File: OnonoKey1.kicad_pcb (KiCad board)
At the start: 2 copper layers, 85 parts, among them SW00 Switch, SW01 Switch, SW02 Switch, SW03 Switch, SW04 Switch, SW05 Switch, SW06 Switch, SW10 Switch, SW11 Switch, SW12 Switch, SW13 Switch, SW14 Switch, SW15 Switch, SW16 Switch, SW20 Switch, SW21 Switch, SW22 Switch, SW23 Switch, SW24 Switch, SW25 Switch, SW26 Switch, SW30 Switch, SW31 Switch, SW32 Switch, SW33 Switch, SW34 Switch, SW35 Switch, SW36 Switch, SW40 Switch, SW41 Switch, SW42 Switch, SW43 Switch, SW44 Switch, SW45 Switch, SW46 Switch, SW50 Switch, SW51 Switch, SW52 Switch, SW53 Switch, SW54 Switch, SW55 Switch, SW56 Switch, U1 RP2040_Zero

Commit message: Changed footprints, rearranged keys on pcb
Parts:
- SW00, SW01, SW02, SW03, SW04, SW05, SW06, SW10, SW11, SW12, SW13, SW14, SW15, SW16, SW20, SW21, SW22, SW23, SW24, SW25, SW26, SW30, SW31, SW32, SW33, SW34, SW35, SW36, SW40, SW41, SW42, SW43, SW44, SW45, SW46, SW50, SW51, SW52, SW53, SW54, SW55, SW56: footprint ScottoKeebs_MX:MX_PCB_1.00u -> Daprice_Keyswitches:Kailh_socket_MX_optional_reversible_1u
- moved SW51 171.1 mm to (60.7, 156.2)
- moved SW41 156.6 mm to (60.7, 137.2)
- moved SW52 154.5 mm to (79.7, 143.2)
- moved SW26 147.3 mm to (155.9, 86.1)
- moved SW31 144.8 mm to (60.7, 118.2)
- moved SW42 144.2 mm to (79.7, 124.2)
- moved SW53 140.7 mm to (98.8, 140.2)
- moved SW32 137.5 mm to (79.7, 105.2)
- moved SW25 136.6 mm to (136.9, 86.1)
- moved SW36 135.2 mm to (155.9, 105.2)
- moved SW43 134.2 mm to (98.8, 121.2)
- moved SW33 132.1 mm to (98.8, 102.2)
- moved SW21 130.7 mm to (60.7, 99.1)
- moved SW22 129.8 mm to (79.7, 86.1)
- moved SW24 129.8 mm to (117.8, 86.1)
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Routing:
- net /COL0: track 177.2 -> 0.00 mm
- net /COL1: track 158.9 -> 0.00 mm
- net /ROW1: track 114.3 -> 0.00 mm
- net /ROW0: track 114.3 -> 0.00 mm
- net /COL6: track 19.1 -> 0.00 mm
- net /COL5: track 19.1 -> 0.00 mm
- net /COL4: track 19.1 -> 0.00 mm
- net /COL3: track 19.1 -> 0.00 mm
- net /COL2: track 19.1 -> 0.00 mm
- net Net-(D6-A): track 8.43 -> 0.00 mm
- net Net-(D4-A): track 8.43 -> 0.00 mm
- net Net-(D2-A): track 8.43 -> 0.00 mm
- net Net-(D13-A): track 8.43 -> 0.00 mm
- net Net-(D1-A): track 8.43 -> 0.00 mm
- net Net-(D8-A): track 8.43 -> 0.00 mm
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
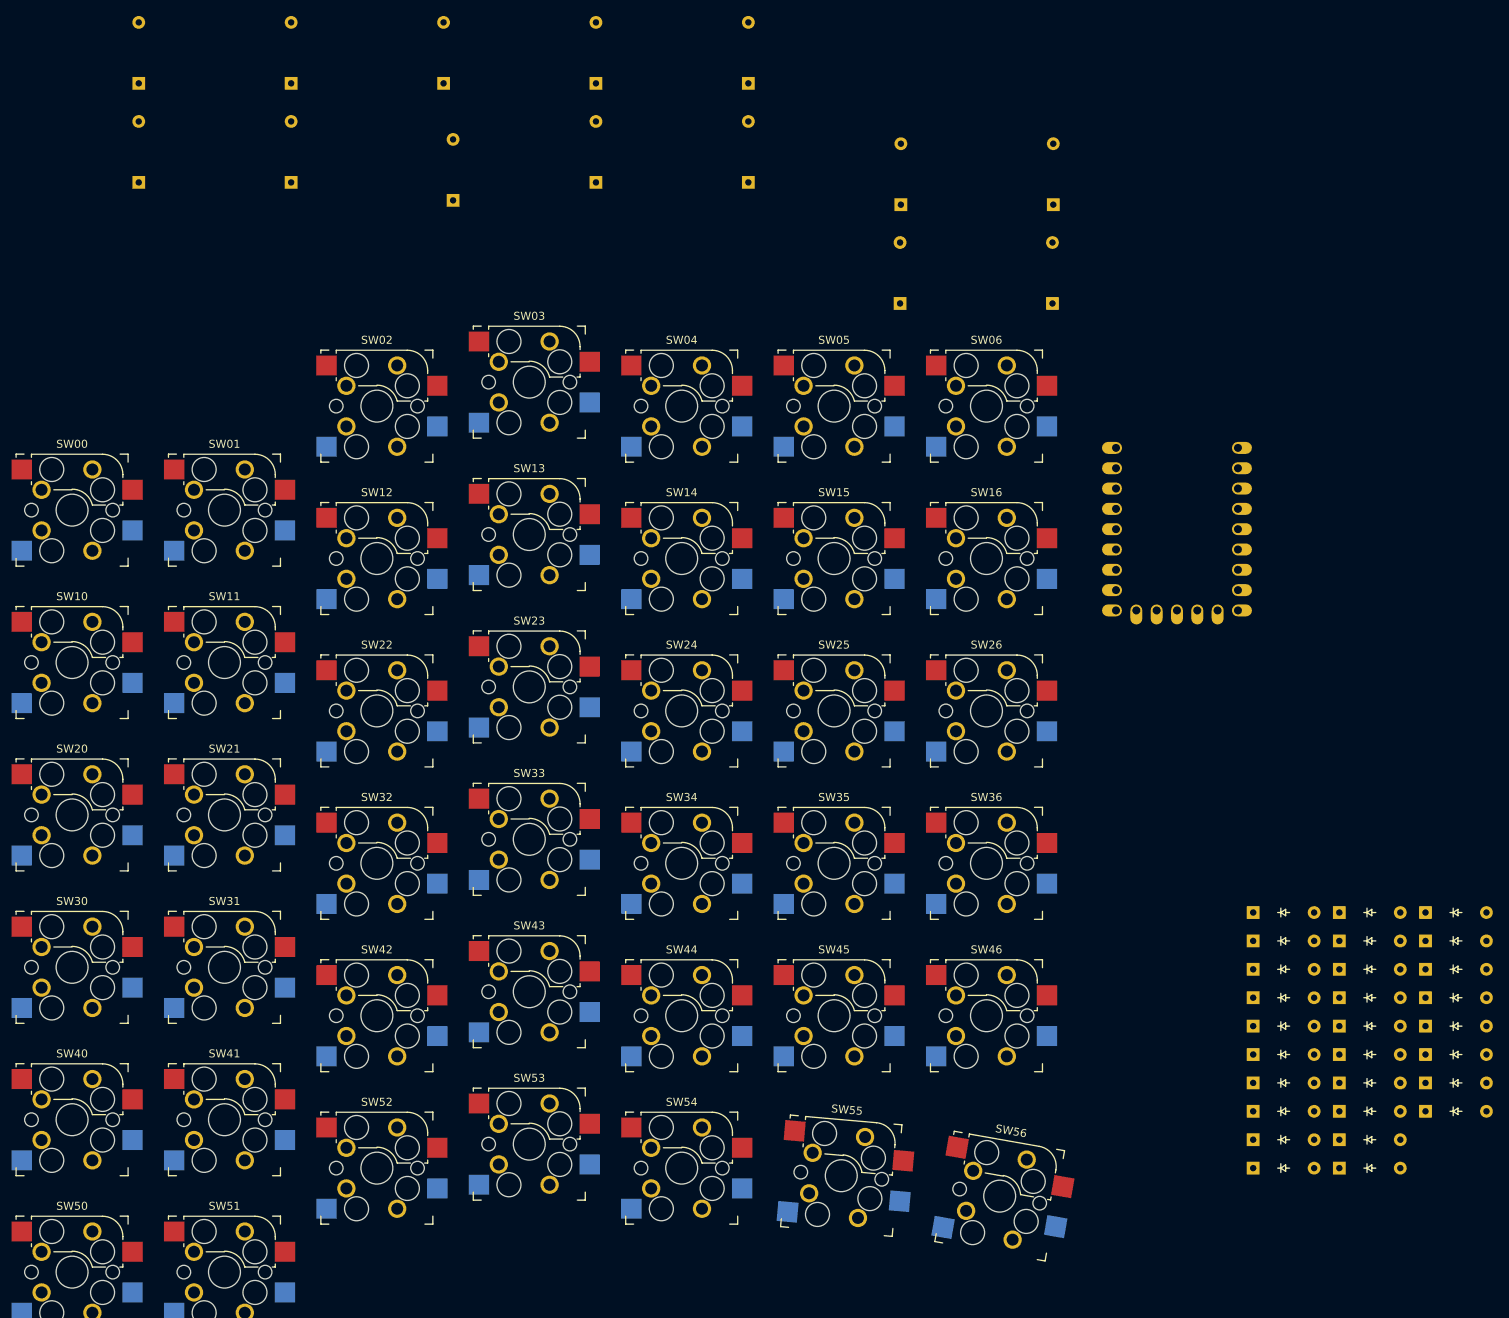
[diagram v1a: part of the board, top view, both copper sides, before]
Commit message: Added M2 holes and two TRRS jacks for front and back
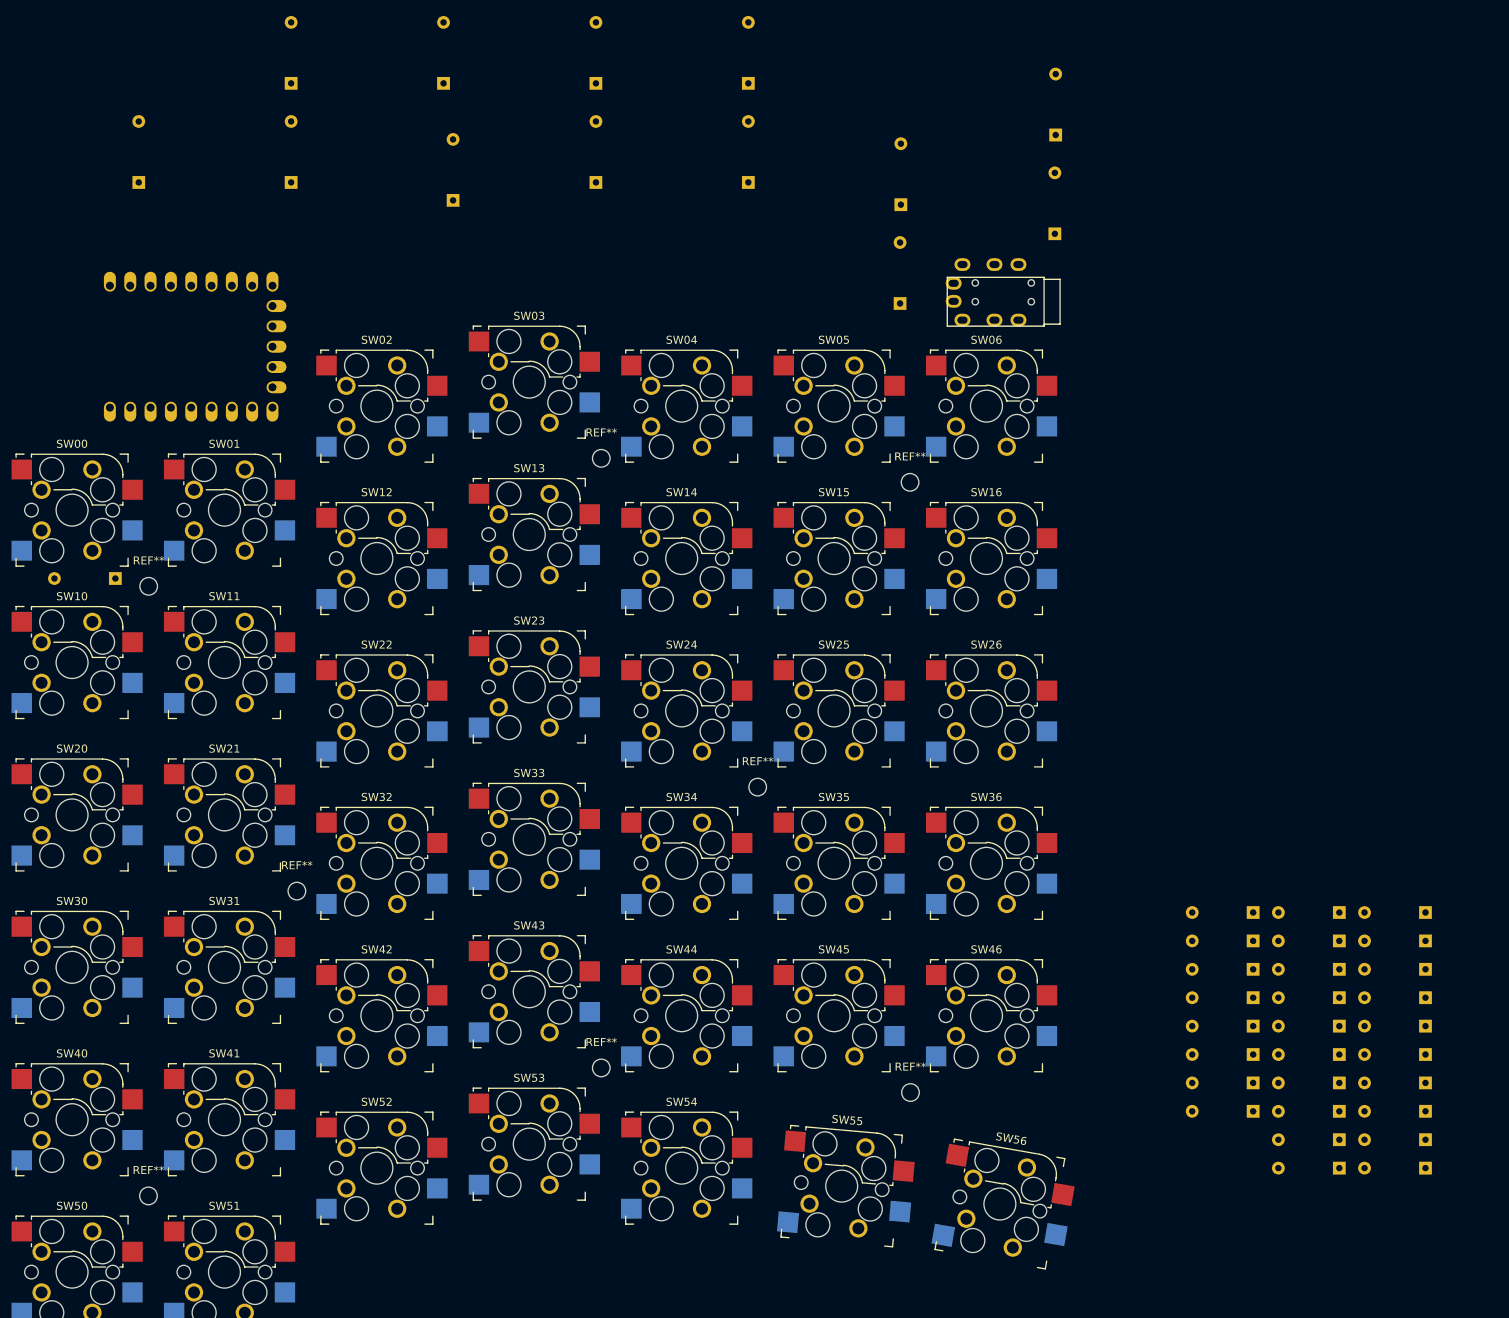
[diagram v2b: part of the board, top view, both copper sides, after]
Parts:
- added REF**: MountingHole_2.2mm_M2, MountingHole:MountingHole_2.2mm_M2, F.Cu at (146.4, 133.8)
- added REF**: MountingHole_2.2mm_M2, MountingHole:MountingHole_2.2mm_M2, F.Cu at (51.2, 70.5)
- added REF**: MountingHole_2.2mm_M2, MountingHole:MountingHole_2.2mm_M2, F.Cu at (146.4, 57.5)
- added REF**: MountingHole_2.2mm_M2, MountingHole:MountingHole_2.2mm_M2, F.Cu at (51.2, 146.7)
- added REF**: MountingHole_2.2mm_M2, MountingHole:MountingHole_2.2mm_M2, F.Cu at (107.8, 130.7)
- added REF**: MountingHole_2.2mm_M2, MountingHole:MountingHole_2.2mm_M2, F.Cu at (69.7, 108.6)
- added REF**: MountingHole_2.2mm_M2, MountingHole:MountingHole_2.2mm_M2, F.Cu at (107.8, 54.5)
- added REF**: MountingHole_2.2mm_M2, MountingHole:MountingHole_2.2mm_M2, F.Cu at (127.3, 95.6)
- added U2: TRRS Front, ScottoKeebs_Components:TRRS_PJ-320A, F.Cu at (163.1, 35.0)
- added U3: TRRS Back, ScottoKeebs_Components:TRRS_PJ-320A, B.Cu at (163.1, 32.6)
- D15, D16, D17, D18, D19, D20, D21, D22, D23, D24, D25, D26, D27, D28, D29, D30, D31, D32, D33, D34, D35, D36, D37, D38, D39, D40, D41, D42: moved to B.Cu
- moved U1 125.3 mm to (56.5, 40.6), turned to 90 degrees
- moved D13 62.0 mm to (47.0, 69.5), turned to 180 degrees
- moved D15 21.5 mm to (210.8, 111.3), turned to 180 degrees
- moved D16 21.5 mm to (210.8, 114.8), turned to 180 degrees
- moved D17 21.5 mm to (210.8, 118.4), turned to 180 degrees
- moved D18 21.5 mm to (210.8, 122.0), turned to 180 degrees
- moved D19 21.5 mm to (210.8, 125.5), turned to 180 degrees
- moved D20 21.5 mm to (210.8, 129.1), turned to 180 degrees
- moved D21 21.5 mm to (210.8, 132.6), turned to 180 degrees
- moved D22 21.5 mm to (210.8, 136.2), turned to 180 degrees
- moved D23 21.5 mm to (210.8, 139.7), turned to 180 degrees
- moved D24 21.5 mm to (210.8, 143.2), turned to 180 degrees
- moved D35 21.5 mm to (189.3, 111.3), turned to 180 degrees
- moved D36 21.5 mm to (189.3, 114.8), turned to 180 degrees
- moved D37 21.5 mm to (189.3, 118.4), turned to 180 degrees
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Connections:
- U1 pad 21: unconnected-(U1-3V3-Pad21) -> 3V3
- U1 pad 22: unconnected-(U1-GND-Pad22) -> GND
- U1 pad 5: unconnected-(U1-4-Pad5) -> /TX1
- U1 pad 6: unconnected-(U1-5-Pad6) -> /RX1

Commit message: some messing around without any result
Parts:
- moved D1 44.8 mm to (67.4, 52.5), turned to 180 degrees
- moved D2 31.7 mm to (86.2, 39.4), turned to 180 degrees
- moved D14 27.7 mm to (40.0, 45.9), turned to 180 degrees
- moved REF** 18.0 mm to (89.8, 54.5)
- moved D13 17.2 mm to (49.9, 52.6)
- moved D11 8.45 mm to (140.7, 28.0)
- moved U2 2.25 mm to (165.4, 35.0)
- moved U3 2.25 mm to (165.4, 32.6)
- moved SW56 1.05 mm to (157.9, 148.8)
- moved D28 0.17 mm to (200.1, 121.8)
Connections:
- U2 pad 1: 3V3 -> GND
- U2 pad 2: GND -> 3V3
- U3 pad 1: 3V3 -> GND
- U3 pad 2: GND -> 3V3
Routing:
- net 3V3: track 0.00 -> 0.57 mm
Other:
- board outline added: 136.9 x 136.5 mm

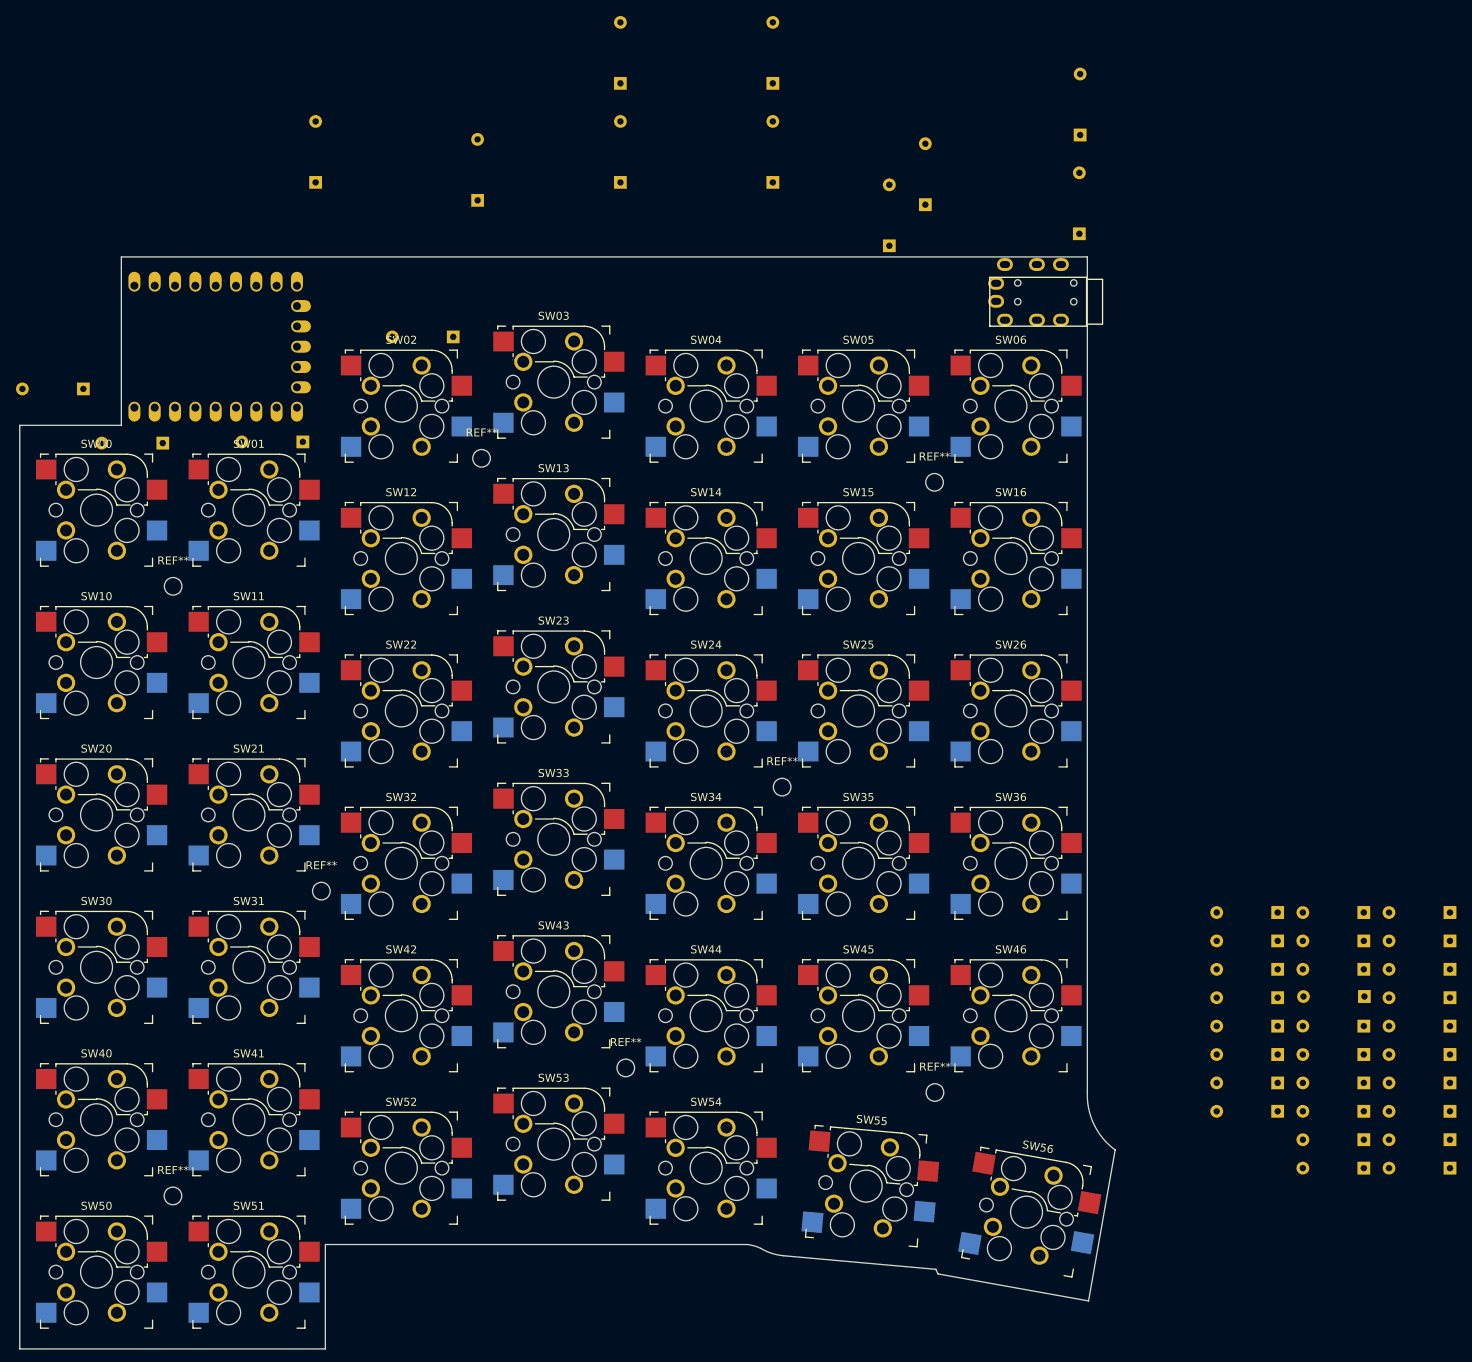
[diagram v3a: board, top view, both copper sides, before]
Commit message: Rearranging board outline, finishing optimising pins for routing, moving upper trrs jack down a little, connecting everything, making DRC errorless
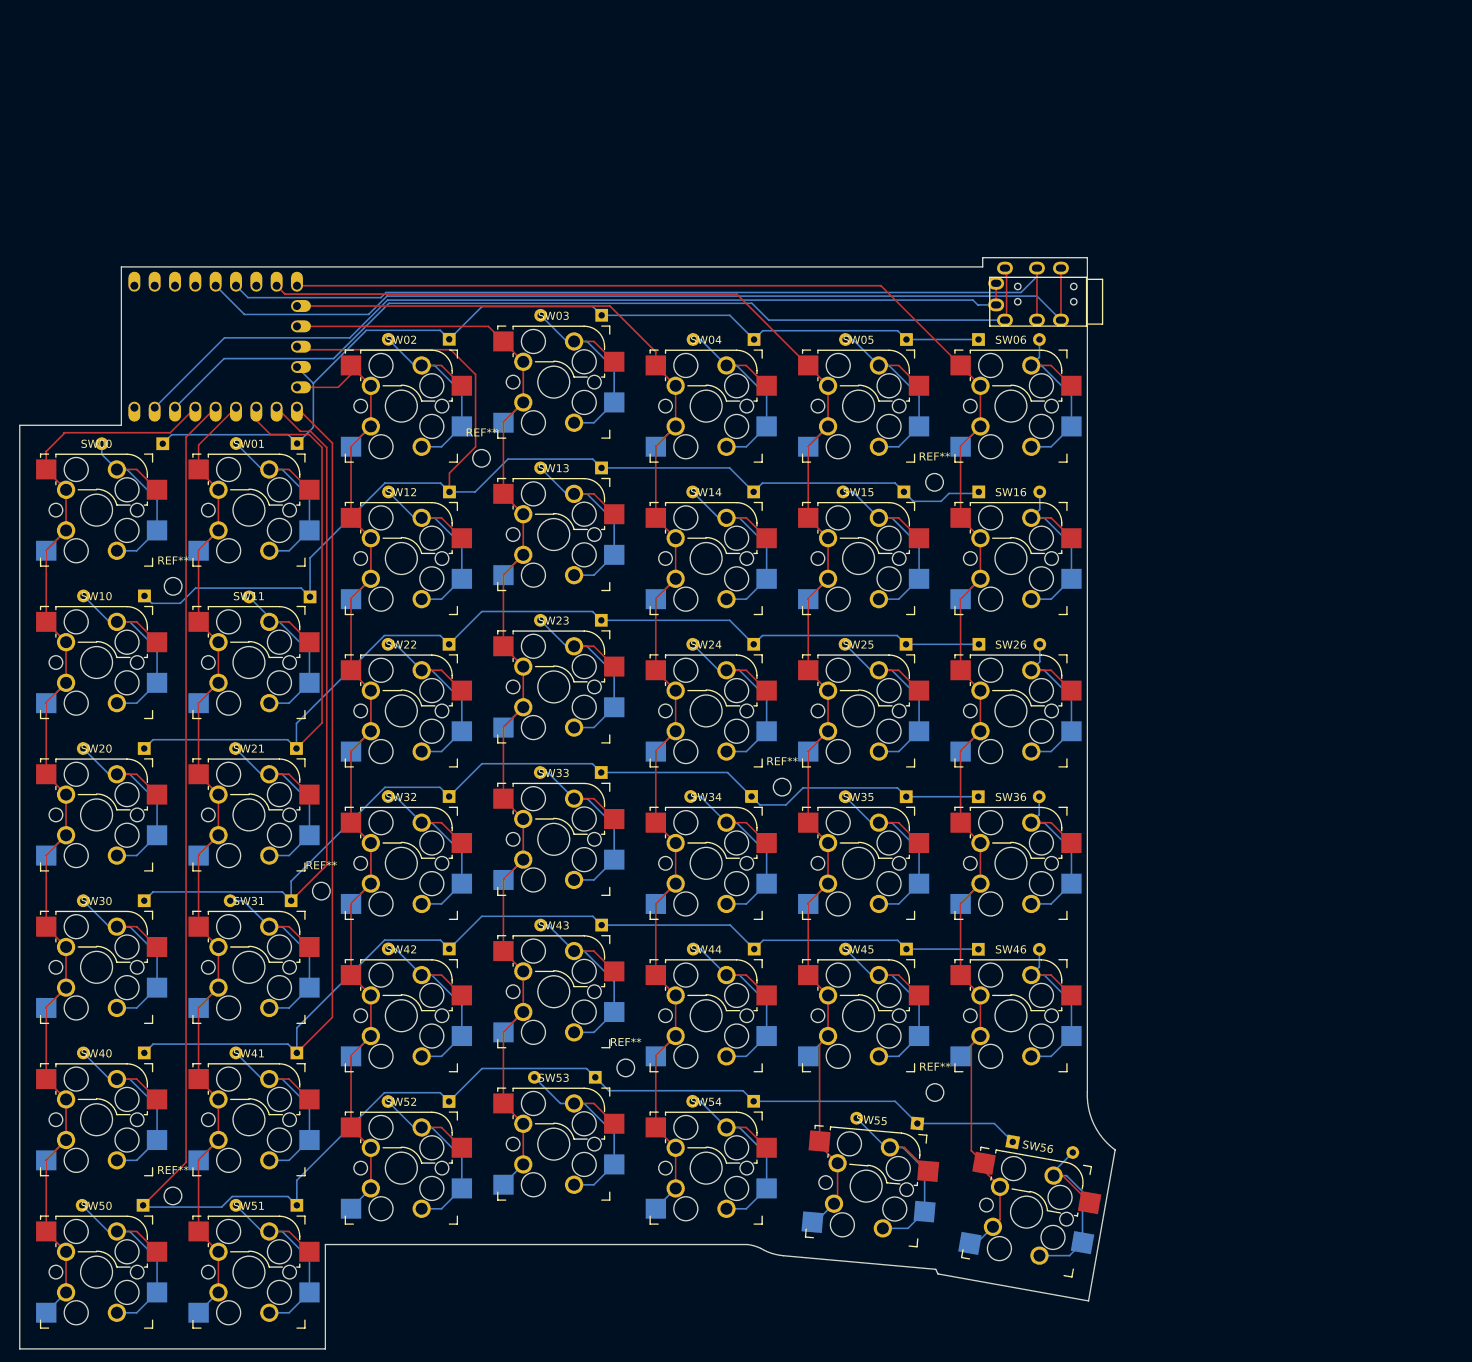
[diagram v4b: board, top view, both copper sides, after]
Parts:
- moved D22 165.3 mm to (47.6, 109.8)
- moved D15 164.5 mm to (47.6, 90.8)
- moved D29 152.5 mm to (47.6, 128.8)
- moved D23 147.9 mm to (66.0, 109.8)
- moved D16 146.2 mm to (66.6, 90.8)
- moved D36 145.6 mm to (47.5, 147.9)
- moved D24 133.4 mm to (85.7, 96.8)
- moved D30 133.4 mm to (66.7, 128.8)
- moved D17 131.5 mm to (85.7, 77.8)
- moved D37 126.1 mm to (66.7, 147.9)
- moved D18 116.1 mm to (104.7, 74.8)
- moved D31 115.5 mm to (85.7, 115.8)
- moved D38 104.4 mm to (85.7, 134.9)
- moved D19 99.3 mm to (123.8, 77.8)
- moved D32 98.1 mm to (104.8, 112.9)
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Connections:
- U1 pad 10: /ROW3 -> /COL4
- U1 pad 11: /ROW2 -> /COL3
- U1 pad 14: /COL6 -> /COL2
- U1 pad 15: /COL5 -> /ROW4
- U1 pad 16: /COL4 -> /ROW3
- U1 pad 17: /COL3 -> /ROW2
- U1 pad 18: /COL2 -> /COL1
- U1 pad 19: /COL1 -> /ROW5
- U1 pad 8: /ROW5 -> /COL5
- U1 pad 9: /ROW4 -> /COL6
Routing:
- net /COL6: track 0.00 -> 227.9 mm
- net /ROW5: track 0.00 -> 226.9 mm
- net /COL5: track 0.00 -> 207.6 mm
- net /ROW4: track 0.00 -> 202.0 mm
- net /ROW3: track 0.00 -> 184.9 mm
- net /COL4: track 0.00 -> 184.5 mm
- net /ROW2: track 0.00 -> 167.9 mm
- net /COL3: track 0.00 -> 162.2 mm
- net /ROW1: track 0.00 -> 160.2 mm
- net /COL0: track 0.00 -> 158.8 mm
- net /COL1: track 0.00 -> 145.2 mm
- net /COL2: track 0.00 -> 144.1 mm
- net /ROW0: track 0.00 -> 119.6 mm
- net 3V3: track 0.57 -> 116.7 mm
- net /TX1: track 0.00 -> 115.8 mm
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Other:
- board size 136.9 x 136.5 mm -> 136.9 x 136.4 mm
